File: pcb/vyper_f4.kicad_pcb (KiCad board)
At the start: 2 copper layers, 30 x 64 mm, 35 parts, among them J1 J1_usb_service_SH4, J2 J2_esc_SH8, J7 J7_swd_testpads, J8 J8_beeper_pads, T1 PAD_T1, T3 PAD_T3, T6 PAD_T6, U1 U1_mcu_STM32F405RGT6, U2 U2_gyro_ICM42688P, U3 U3_buck_TPS54360, U4 U4_ldo_3v3, U5 U5_gyro_ldo_AP2112K, U6 U6_flash_W25Q128, U7 U7_baro_BMP280, U8 U8_rgb_level_shifter, Y1 Y1_xtal_8MHz

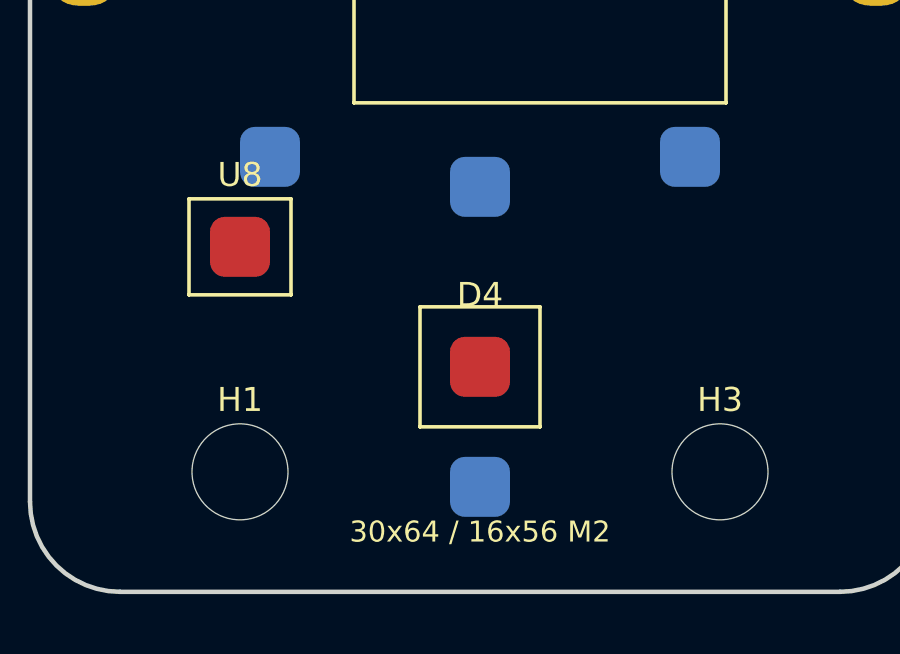
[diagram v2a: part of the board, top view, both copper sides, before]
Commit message: Specify exact FC USB protection
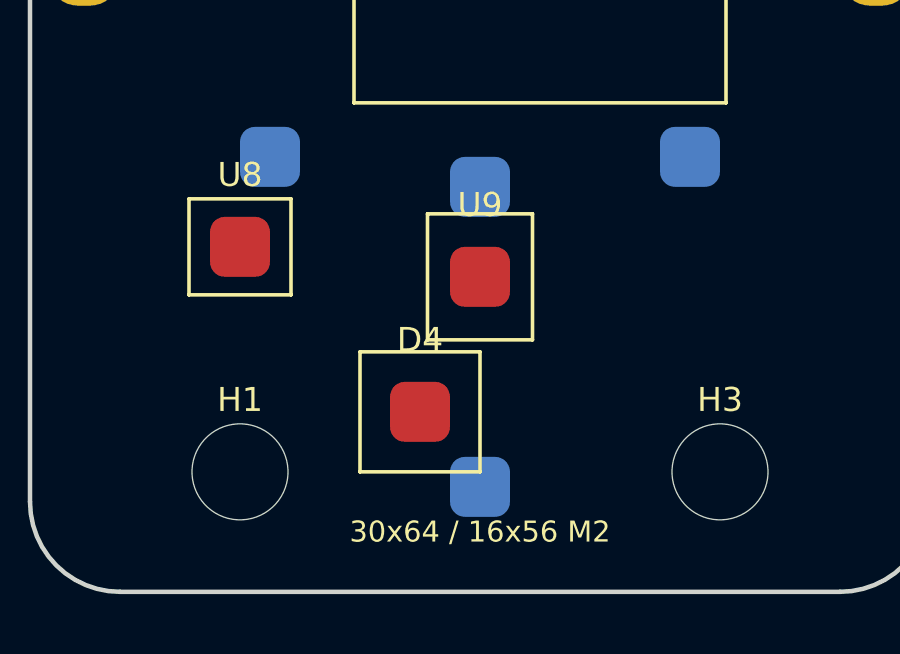
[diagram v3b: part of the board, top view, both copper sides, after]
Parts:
- added U9: U9_usb_esd_USBLC6, VYPER:U9_usb_esd_USBLC6, F.Cu at (0.00, 21.5)
- moved D4 2.50 mm to (-2.00, 26.0)
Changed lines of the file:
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@@
 		(pad "1" smd roundrect (at 0.000 0.000) (size 2.0 2.0) (layers "F.Cu" "F.Paste" "F.Mask") (roundrect_rratio 0.25))
 	)
-	(gr_rect (start -2.000 22.500) (end 2.000 26.500) (stroke (width 0.05) (type solid)) (fill no) (layer "F.CrtYd"))
-	(gr_rect (start -2.000 22.500) (end 2.000 26.500) (stroke (width 0.12) (type solid)) (fill no) (layer "F.SilkS"))
+	(gr_rect (start -1.750 19.400) (end 1.750 23.600) (stroke (width 0.05) (type solid)) (fill no) (layer "F.CrtYd"))
+	(gr_rect (start -1.750 19.400) (end 1.750 23.600) (stroke (width 0.12) (type solid)) (fill no) (layer "F.SilkS"))
+	(footprint "VYPER:U9_usb_esd_USBLC6" (layer "F.Cu")
+		(at 0.000 21.500)
+		(attr exclude_from_pos_files)
+		(property "Reference" "U9" (at 0 -2.4 0) (layer "F.SilkS")
+			(effects (font (size 0.8 0.8) (thickness 0.12)))
+		)
+		(property "Value" "U9_usb_esd_USBLC6" (at 0 2.4 0) (layer "F.SilkS")
+			(effects (font (size 0.5 0.5) (thickness 0.08)) (hide yes))
+		)
+		(pad "1" smd roundrect (at 0.000 0.000) (size 2.0 2.0) (layers "F.Cu" "F.Paste" "F.Mask") (roundrect_rratio 0.25))
+	)
+	(gr_rect (start -4.000 24.000) (end 0.000 28.000) (stroke (width 0.05) (type solid)) (fill no) (layer "F.CrtYd"))
+	(gr_rect (start -4.000 24.000) (end 0.000 28.000) (stroke (width 0.12) (type solid)) (fill no) (layer "F.SilkS"))
 	(footprint "VYPER:D4_rgb_status" (layer "F.Cu")
-		(at 0.000 24.500)
+		(at -2.000 26.000)
 		(attr exclude_from_pos_files)
 		(property "Reference" "D4" (at 0 -2.4 0) (layer "F.SilkS")

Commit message: Route and match Vyper FC USB
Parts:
- moved D4 2.24 mm to (0.00, 27.0)
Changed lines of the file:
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@@
 		(pad "1" smd roundrect (at 0.000 0.000) (size 2.0 2.0) (layers "F.Cu" "F.Paste" "F.Mask") (roundrect_rratio 0.25))
 	)
-	(gr_rect (start -4.000 24.000) (end 0.000 28.000) (stroke (width 0.05) (type solid)) (fill no) (layer "F.CrtYd"))
-	(gr_rect (start -4.000 24.000) (end 0.000 28.000) (stroke (width 0.12) (type solid)) (fill no) (layer "F.SilkS"))
+	(gr_rect (start -2.000 25.000) (end 2.000 29.000) (stroke (width 0.05) (type solid)) (fill no) (layer "F.CrtYd"))
+	(gr_rect (start -2.000 25.000) (end 2.000 29.000) (stroke (width 0.12) (type solid)) (fill no) (layer "F.SilkS"))
 	(footprint "VYPER:D4_rgb_status" (layer "F.Cu")
-		(at -2.000 26.000)
+		(at 0.000 27.000)
 		(attr exclude_from_pos_files)
 		(property "Reference" "D4" (at 0 -2.4 0) (layer "F.SilkS")
